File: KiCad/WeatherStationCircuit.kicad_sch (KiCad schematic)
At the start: 5 parts, among them U1 DHT11, U2 DS1307+, U3 BMP280

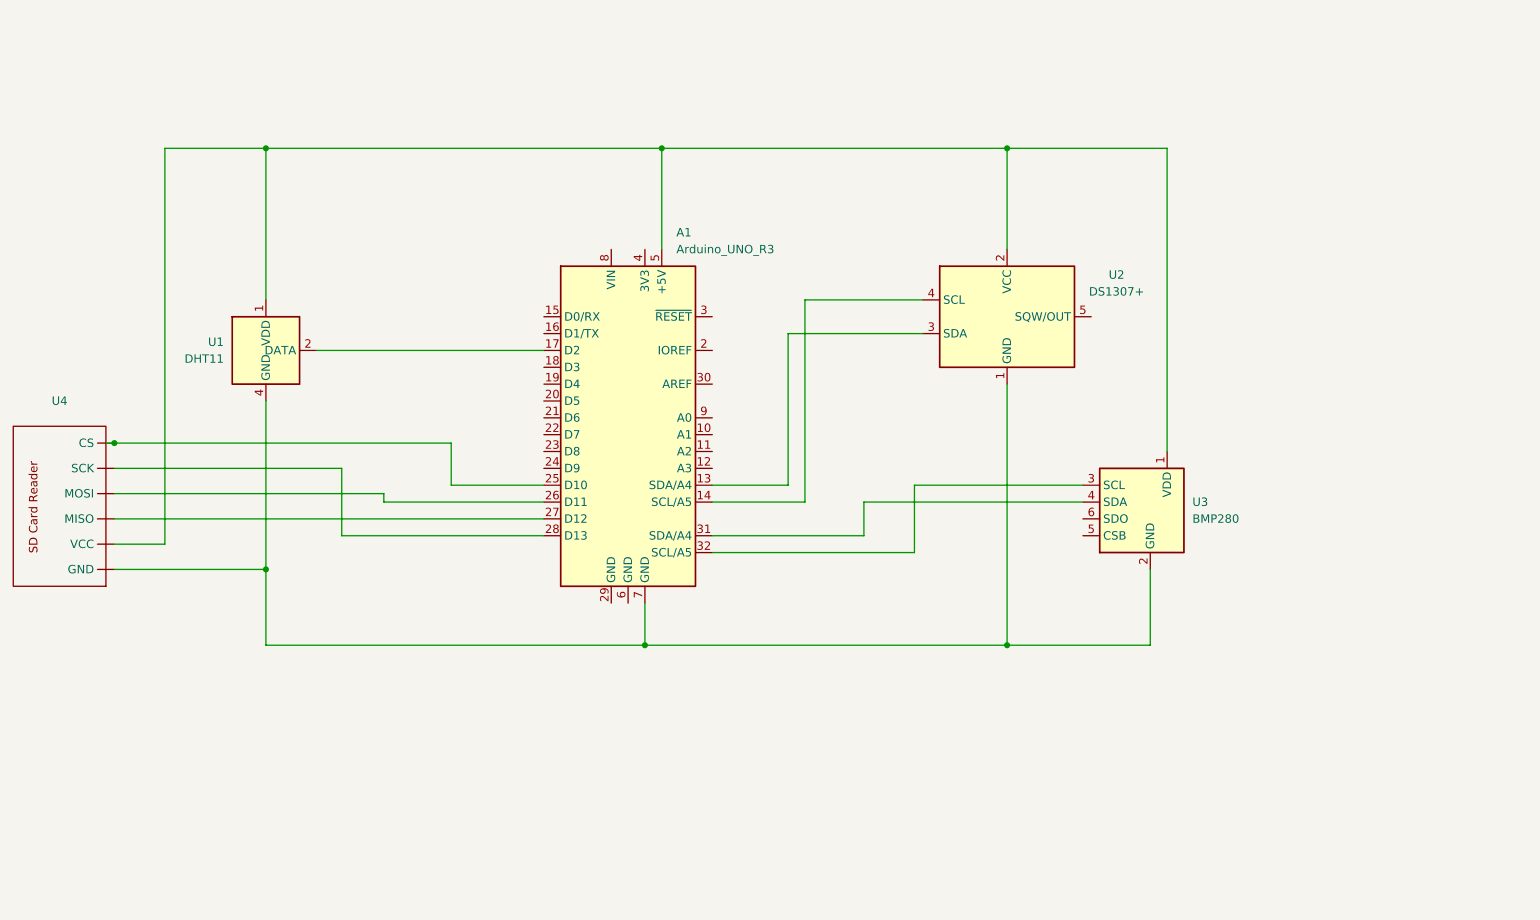
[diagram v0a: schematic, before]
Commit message: expanded the circuit diagram involving the extra sensors and LCD. gotta work on making the code more modular.
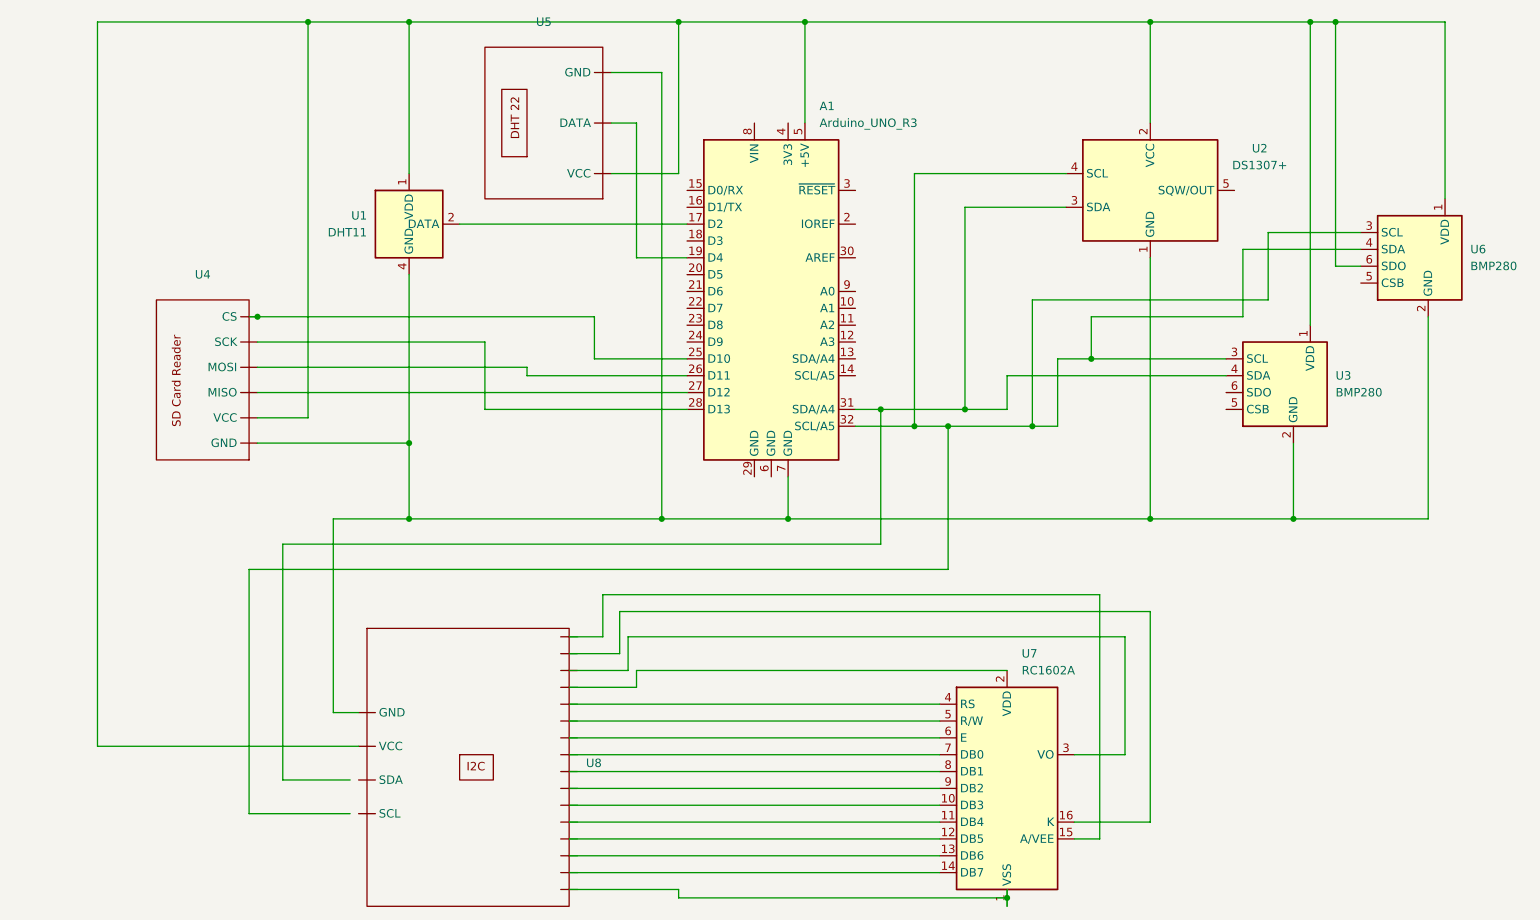
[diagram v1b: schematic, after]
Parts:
- added U5: ~, symbol DHT22:DHT22
- added U6: BMP280, Package_LGA:Bosch_LGA-8_2x2.5mm_P0.65mm_ClockwisePinNumbering, symbol Sensor_Pressure:BMP280
- added U7: RC1602A, Display:RC1602A, symbol Display_Character:RC1602A
- added U8: ~, symbol Display_Character:I2C
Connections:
- net GND: now also U6.7 (GND)
- net VDDIO: now also U6.6 (VDDIO)
- net at A1.13 (SDA/A4): no longer U2.3 (SDA)
- net at U2.4 (SCL): now also A1.32 (SCL/A5), U3.3 (SCL), U6.3 (SCL), U6.4 (SDA); no longer A1.14 (SCL/A5)
- net at A1.19 (D4): now also U5. (VCC)
- net at A1.31 (SDA/A4), U3.4 (SDA): now also U2.3 (SDA)
- net at A1.5 (+5V), U1.1 (VDD), U2.2 (VCC)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: now also U5. (VCC), U6.1 (VDD), U6.6 (VDDIO), U8. (VCC)
- net at A1.7 (GND), U1.4 (GND), U2.1 (GND)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: now also U5. (VCC), U6.2 (GND), U8. (VCC)
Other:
- moved on the sheet: A1, U1, U2, U3, U4
